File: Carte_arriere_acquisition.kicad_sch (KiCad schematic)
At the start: 17 parts, among them J1 Screw_Terminal_01x02, J2 Vers_BMS, J3 Vers_Thermistor, J4 Vers_Capteur_Hall, J5 Conn_01x04_Pin, J6 Conn_01x04_Pin, U1 ESP32-DEVKITC-32E, U2 SN65HVD230, U3 MAX3485, U4 module_mpu6050

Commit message: modif
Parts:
- added C4: C, symbol Device:C
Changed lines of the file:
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@@
+	)
+	(symbol
+		(lib_id "Device:C")
+		(at 232.41 60.96 0)
+		(unit 1)
+		(exclude_from_sim no)
+		(in_bom yes)
+		(on_board yes)
+		(dnp no)
+		(fields_autoplaced yes)
+		(property "Reference" "C4"
+			(at 236.22 59.6899 0)
+			(effects
+				(font
+					(size 1.27 1.27)
+				)
+				(justify left)
+			)
+		)
+		(property "Value" "C"
+			(at 236.22 62.2299 0)
+			(effects
+				(font
+					(size 1.27 1.27)
+				)
+				(justify left)
+			)
+		)
+		(property "Footprint" ""
+			(at 233.3752 64.77 0)
+			(effects
+				(font
+					(size 1.27 1.27)
+				)
+				(hide yes)
+			)
+		)
+		(property "Datasheet" "~"
+			(at 232.41 60.96 0)
+			(effects
+				(font
+					(size 1.27 1.27)
+				)
+				(hide yes)
+			)
+		)
+		(property "Description" "Unpolarized capacitor"
+			(at 232.41 60.96 0)
+			(effects
+				(font
+					(size 1.27 1.27)
+				)
+				(hide yes)
+			)
+		)
+		(pin "2"
+		)
+		(pin "1"
+		)
+		(instances
+			(project ""
+				(path "/fb38ad7d-e898-4985-b7ba-f83eff01a74e"
+					(reference "C4")
+					(unit 1)
+				)
+			)
+		)
 	)
 	(symbol

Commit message: Modif PCB
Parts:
- removed C1: 100nF, Capacitor_SMD:C_0805_2012Metric_Pad1.18x1.45mm_HandSolder, symbol Device:C
- removed C4: C, symbol Device:C
- removed J3: Vers_Thermistor, TerminalBlock_Phoenix:TerminalBlock_Phoenix_MKDS-1,5-2_1x02_P5.00mm_Horizontal, symbol Connector:Screw_Terminal_01x02
- removed J5, J6: Conn_01x04_Pin, Connector_PinHeader_1.27mm:PinHeader_1x04_P1.27mm_Vertical, symbol Connector:Conn_01x04_Pin
- removed TH1: Thermistor_NTC, symbol Device:Thermistor_NTC
- removed U1: ESP32-DEVKITC-32E, ESP32-DEVKITC-32E:MODULE_ESP32-DEVKITC-32E, symbol ESP32-DEVKITC-32E:ESP32-DEVKITC-32E
- removed U4: module_mpu6050, usini_sensors:module_mpu6050, symbol usini_sensors:module_mpu6050
- added D1, D2, D3: 1N4007, Diode_THT:D_DO-41_SOD81_P10.16mm_Horizontal, symbol Diode:1N4007
- added J3: ACCEL_VEVOR, symbol Connector_Generic:Conn_01x03
- added J5: Arrivée_Regulateur, symbol Connector:Screw_Terminal_01x03
- added J6: Conn_Feu_Stop, symbol Connector:Screw_Terminal_01x02
- added J7: Conn_Cligno_G, symbol Connector:Screw_Terminal_01x02
- added J8: Conn_Cligno_D, symbol Connector:Screw_Terminal_01x02
- added J9: Conn_Capt_Courant, symbol Connector:Screw_Terminal_01x03
- added Q1, Q2, Q3: IRLZ44N, Package_TO_SOT_THT:TO-220-3_Vertical, symbol Transistor_FET:IRLZ44N
- added R4, R6, R8: 220, symbol Device:R
- added R5, R7, R9: 10k, symbol Device:R
- added U1: MCP4725xxx-xCH, Package_TO_SOT_SMD:SOT-23-6, symbol Analog_DAC:MCP4725xxx-xCH
- added U4: DS18B20, Package_TO_SOT_THT:TO-92_Inline, symbol Sensor_Temperature:DS18B20
- added U5: BOB-12009, BOB-12009:CONV_BOB-12009, symbol BOB-12009:BOB-12009
- added U6: ESP32-DEVKIT-V1, ESP32-DEVKIT-V1:MODULE_ESP32_DEVKIT_V1, symbol ESP32-DEVKIT-V1:ESP32-DEVKIT-V1
- C2, C3: footprint Capacitor_SMD:C_0805_2012Metric_Pad1.18x1.45mm_HandSolder -> (none)
- J1, J2: footprint TerminalBlock_Phoenix:TerminalBlock_Phoenix_MKDS-1,5-2_1x02_P5.00mm_Horizontal -> (none)
- J4: footprint TerminalBlock_Phoenix:TerminalBlock_Phoenix_MKDS-1,5-3_1x03_P5.00mm_Horizontal -> (none)
- R1, R2, R3: footprint Resistor_SMD:R_0805_2012Metric_Pad1.20x1.40mm_HandSolder -> (none)
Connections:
- net +3.3V: now also J9.1 (Pin_1), U4.3 (V_{DD}), U5.LV, U6.1 (3V3)
- net +5V: now also J5.2 (Pin_2), U1.3 (VDD), U5.HV, U6.30 (VIN)
- net BMS RX: now also U6.13 (TX0)
- net BMS TX: now also U6.12 (RX0)
- net BMS_Direction: now also U6.25 (D27)
- net CAN_RX: now also U6.5 (D4)
- net CAN_TX: now also U6.8 (D5)
- net GND: now also J3.2 (Pin_2), J5.3 (Pin_3), J9.2 (Pin_2), Q1.3 (S), Q2.3 (S), Q3.3 (S), R5.2, R7.2, R9.2, U1.2 (VSS), U1.6 (A0), U4.1 (GND), U5.GND_1 (GND), U5.GND_2 (GND), U6.2 (GND), U6.29 (GND)
- net SCL: now also U5.LV2, U6.14 (D22)
- net SDA: now also U5.LV1, U6.11 (D21)
- net at R2.1, U2.7 (CANH): now also J1.1 (Pin_1); no longer J1.2 (Pin_2)
- net at R2.2, U2.6 (CANL): now also J1.2 (Pin_2); no longer J1.1 (Pin_1)
- net Hall renamed V_rotation
- net V_rotation: now also U6.26 (D14)
- new net: D1.2 (A), J6.2 (Pin_2), Q1.2 (D)
- new net: D3.2 (A), J8.2 (Pin_2), Q3.2 (D)
- new net: Q1.1 (G), R4.2, R5.1
- new net: D2.2 (A), J7.2 (Pin_2), Q2.2 (D)
- new net: J3.1 (Pin_1), U1.1 (VOUT)
- new net: Q3.1 (G), R8.2, R9.1
- new net: Q2.1 (G), R6.2, R7.1
- new net +12V: D1.1 (K), D2.1 (K), D3.1 (K), J5.1 (Pin_1), J6.1 (Pin_1), J7.1 (Pin_1), J8.1 (Pin_1)
- new net CMD_CLIGNO_D: R8.1, U6.28 (D13)
- new net CMD_CLIGNO_G: R6.1, U6.27 (D12)
- new net CMD_STOP: R4.1, U6.4 (D2)
- new net Courant: J9.3 (Pin_3), U6.19 (D34)
- new net SCL_MCP: U1.5 (SCL), U5.HV2
- new net SDA_MCP: U1.4 (SDA), U5.HV1
- new net Temp: U4.2 (DQ), U6.3 (D15)
- no-connect marks 25 -> 0
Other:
- moved on the sheet: C2, C3, J1, J2, J4, R1, R2, R3, U2, U3

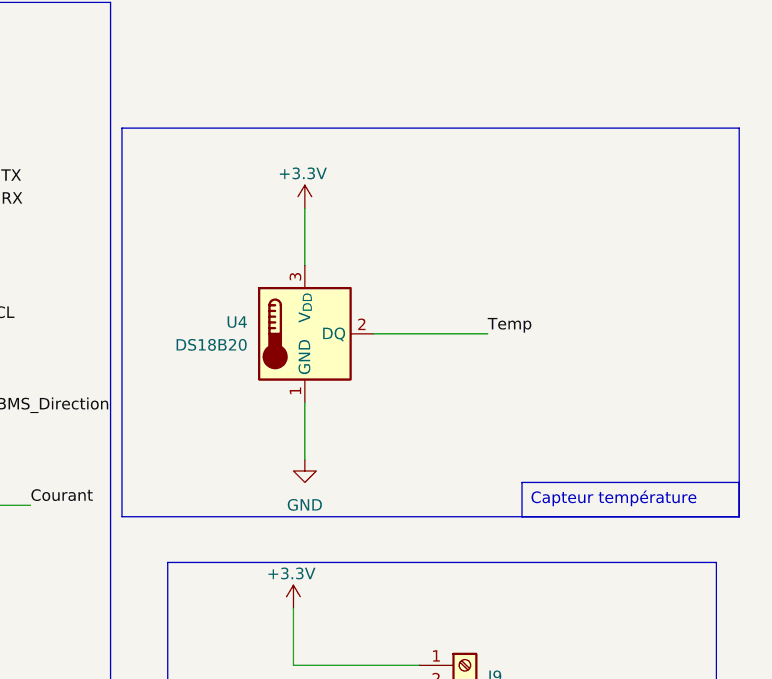
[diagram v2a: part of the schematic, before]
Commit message: Changement capteur temp
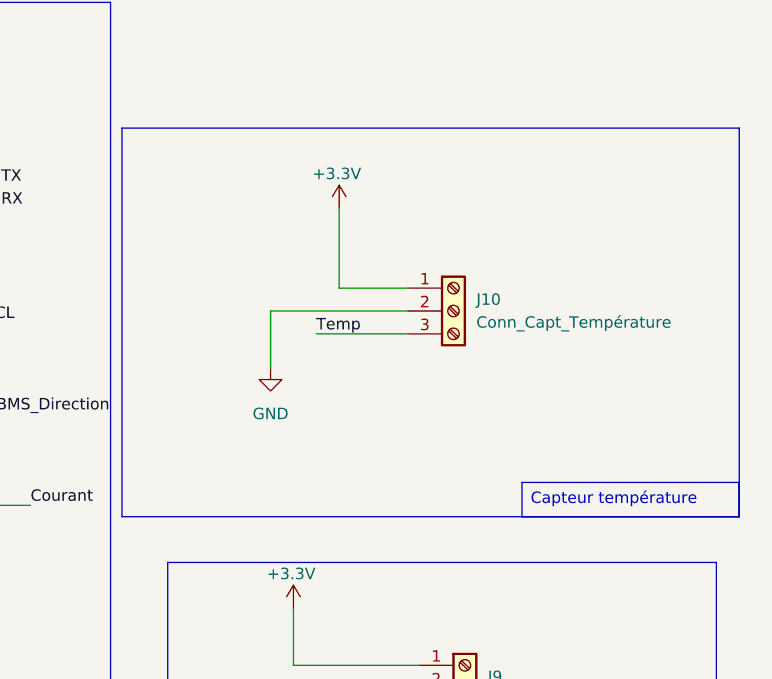
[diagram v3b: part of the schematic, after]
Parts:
- removed U4: DS18B20, Package_TO_SOT_THT:TO-92_Inline, symbol Sensor_Temperature:DS18B20
- added J10: Conn_Capt_Température, symbol Connector:Screw_Terminal_01x03
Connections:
- net +3.3V: now also J10.1 (Pin_1)
- net GND: now also J10.2 (Pin_2)
- net Temp: now also J10.3 (Pin_3)
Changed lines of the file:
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@@
 	(wire
 		(pts
-			(xy 236.22 35.56) (xy 236.22 41.91)
-		)
-		(stroke
-			(width 0)
-			(type default)
-		)
-	)
-	(wire
-		(pts
 			(xy 29.21 48.26) (xy 46.99 48.26)
 		)
@@
 	(wire
 		(pts
+			(xy 240.03 44.45) (xy 247.65 44.45)
+		)
+		(stroke
+			(width 0)
+			(type default)
+		)
+	)
+	(wire
+		(pts
 			(xy 20.32 22.86) (xy 46.99 22.86)
 		)
@@
 	(wire
 		(pts
-			(xy 243.84 49.53) (xy 256.54 49.53)
-		)
-		(stroke
-			(width 0)
-			(type default)
-		)
-	)
-	(wire
-		(pts
 			(xy 228.6 138.43) (xy 237.49 138.43)
 		)
@@
 	(wire
 		(pts
-			(xy 236.22 57.15) (xy 236.22 63.5)
+			(xy 232.41 46.99) (xy 232.41 53.34)
 		)
 		(stroke
@@
 	(wire
 		(pts
+			(xy 237.49 49.53) (xy 247.65 49.53)
+		)
+		(stroke
+			(width 0)
+			(type default)
+		)
+	)
+	(wire
+		(pts
 			(xy 25.4 86.36) (xy 60.96 86.36)
 		)
@@
 	(wire
 		(pts
+			(xy 240.03 35.56) (xy 240.03 44.45)
+		)
+		(stroke
+			(width 0)
+			(type default)
+		)
+	)
+	(wire
+		(pts
 			(xy 196.85 24.13) (xy 196.85 25.4)
 		)
@@
 	(wire
 		(pts
+			(xy 232.41 46.99) (xy 247.65 46.99)
+		)
+		(stroke
+			(width 0)
+			(type default)
+		)
+	)
+	(wire
+		(pts
 			(xy 73.66 182.88) (xy 78.74 182.88)
 		)
@@
 		)
 	)
-	(label "Temp"
-		(at 256.54 49.53 0)
-		(effects
-			(font
-				(size 1.27 1.27)
-			)
-			(justify left bottom)
-		)
-	)
 	(label "CMD_CLIGNO_G"
 		(at 152.4 55.88 0)
@@
 		)
 	)
+	(label "Temp"
+		(at 237.49 49.53 0)
+		(effects
+			(font
+				(size 1.27 1.27)
+			)
+			(justify left bottom)
+		)
+	)
 	(label "BMS TX"
 		(at 198.12 33.02 0)
@@
 	)
 	(symbol
-		(lib_id "Sensor_Temperature:DS18B20")
-		(at 236.22 49.53 0)
+		(lib_id "Connector:Screw_Terminal_01x03")
+		(at 252.73 46.99 0)
 		(unit 1)
 		(exclude_from_sim no)
@@
 		(dnp no)
 		(fields_autoplaced yes)
-		(property "Reference" "U4"
-			(at 229.87 48.2599 0)
+		(property "Reference" "J10"
+			(at 255.27 45.7199 0)
 			(effects
 				(font
 					(size 1.27 1.27)
 				)
-				(justify right)
+				(justify left)
 			)
 		)
-		(property "Value" "DS18B20"
-			(at 229.87 50.7999 0)
+		(property "Value" "Conn_Capt_Température"
+			(at 255.27 48.2599 0)
 			(effects
 				(font
 					(size 1.27 1.27)
 				)
-				(justify right)
+				(justify left)
 			)
 		)
-		(property "Footprint" "Package_TO_SOT_THT:TO-92_Inline"
-			(at 210.82 55.88 0)
+		(property "Footprint" ""
+			(at 252.73 46.99 0)
 			(effects
 				(font
@@
 			)
 		)
-		(property "Datasheet" "http://datasheets.maximintegrated.com/en/ds/DS18B20.pdf"
-			(at 232.41 43.18 0)
+		(property "Datasheet" "~"
+			(at 252.73 46.99 0)
 			(effects
 				(font
@@
 			)
 		)
-		(property "Description" "Programmable Resolution 1-Wire Digital Thermometer TO-92"
-			(at 236.22 49.53 0)
+		(property "Description" "Generic screw terminal, single row, 01x03, script generated (kicad-library-utils/schlib/autogen/connector/)"
+			(at 252.73 46.99 0)
 			(effects
 				(font
@@
 			)
 		)
-		(pin "2"
-		)
 		(pin "1"
 		)
 		(pin "3"
 		)
+		(pin "2"
+		)
 		(instances
 			(project "Carte_arriere_acquisition"
 				(path "/fb38ad7d-e898-4985-b7ba-f83eff01a74e"
-					(reference "U4")
+					(reference "J10")
 					(unit 1)
 				)
@@
 	(symbol
 		(lib_id "power:+3.3V")
-		(at 236.22 35.56 0)
+		(at 240.03 35.56 0)
 		(unit 1)
 		(exclude_from_sim no)
@@
 		(dnp no)
 		(property "Reference" "#PWR014"
-			(at 236.22 39.37 0)
+			(at 240.03 39.37 0)
 			(effects
 				(font
@@
 		)
 		(property "Value" "+3.3V"
-			(at 235.966 31.75 0)
+			(at 239.776 31.75 0)
 			(effects
 				(font
@@
 		)
 		(property "Footprint" ""
-			(at 236.22 35.56 0)
+			(at 240.03 35.56 0)
 			(effects
 				(font
@@
 		)
 		(property "Datasheet" ""
-			(at 236.22 35.56 0)
+			(at 240.03 35.56 0)
 			(effects
 				(font
@@
 		)
 		(property "Description" "Power symbol creates a global label with name \"+3.3V\""
-			(at 236.22 35.56 0)
+			(at 240.03 35.56 0)
 			(effects
 				(font
@@
 	(symbol
 		(lib_id "power:GND")
-		(at 236.22 63.5 0)
+		(at 232.41 53.34 0)
 		(unit 1)
 		(exclude_from_sim no)
@@
 		(fields_autoplaced yes)
 		(property "Reference" "#PWR013"
-			(at 236.22 69.85 0)
+			(at 232.41 59.69 0)
 			(effects
 				(font
@@
 		)
 		(property "Value" "GND"
-			(at 236.22 68.58 0)
+			(at 232.41 58.42 0)
 			(effects
 				(font
@@
 		)
 		(property "Footprint" ""
-			(at 236.22 63.5 0)
+			(at 232.41 53.34 0)
 			(effects
 				(font
@@
 		)
 		(property "Datasheet" ""
-			(at 236.22 63.5 0)
+			(at 232.41 53.34 0)
 			(effects
 				(font
@@
 		)
 		(property "Description" "Power symbol creates a global label with name \"GND\" , ground"
-			(at 236.22 63.5 0)
+			(at 232.41 53.34 0)
 			(effects
 				(font

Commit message: ajout IMU
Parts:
- added U4: module_mpu6050, usini_sensors:module_mpu6050, symbol usini_sensors:module_mpu6050
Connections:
- net +5V: now also U4.1 (VCC)
- net GND: now also U4.2 (GND)
- net SCL: now also U4.3 (SCL)
- net SDA: now also U4.4 (SDA)
- net INT: now reaches U6.15 (D23)
- net INT: now also U4.8 (INT)
